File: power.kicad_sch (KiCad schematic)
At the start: 13 parts, among them P1 USB_C_Plug_USB2.0, Q1 FS8205A, U2 TP4056-42-ESOP8, U3 DW01A

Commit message: update
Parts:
- C1, C2: footprint (none) -> Capacitor_SMD:C_0805_2012Metric_Pad1.18x1.45mm_HandSolder
- D85, D86: footprint (none) -> LED_SMD:LED_0805_2012Metric_Pad1.15x1.40mm_HandSolder
- P1: footprint (none) -> Connector_USB:USB_C_Receptacle_GCT_USB4105-xx-A_16P_TopMnt_Horizontal
- R1, R2, R3, R4, R5: footprint (none) -> Resistor_SMD:R_0805_2012Metric_Pad1.20x1.40mm_HandSolder

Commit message: almost done
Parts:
- added D87: LED, LED_SMD:LED_0805_2012Metric_Pad1.15x1.40mm_HandSolder, symbol Device:LED
- added J3: Conn_01x02_Pin, Connector_JST:JST_PH_B2B-PH-K_1x02_P2.00mm_Vertical, symbol Connector:Conn_01x02_Pin
- added R7: 1k, Resistor_SMD:R_0805_2012Metric_Pad1.20x1.40mm_HandSolder, symbol Device:R
- added SW88: SW_SPDT, Button_Switch_THT:SW_Slide_SPDT_Angled_CK_OS102011MA1Q, symbol Switch:SW_SPDT
- added U4: MCP1700x-330xxTT, Package_TO_SOT_SMD:SOT-23W_Handsoldering, symbol Regulator_Linear:MCP1700x-330xxTT
- C2: value C -> 0.1u
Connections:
- net B- is gone; now on net -BATT: C1.2, Q1.2, Q1.3, U3.6 (GND)
- net VCC is gone; now on net +BATT: R1.1
- net +BATT: now also U2.5 (BAT), J3.1 (Pin_1), SW88.2 (B)
- net -BATT: now also J3.2 (Pin_2)
- net GND: now also R7.2, U4.1 (GND)
- net USB_D+: now reaches P1.A6 (D+)
- net USB_D-: now reaches P1.A7 (D-)
- new net: SW88.1 (A), U4.3 (VI)
- new net: D87.1 (K), R7.1
- new net +3.3V: D87.2 (A), U4.2 (VO)

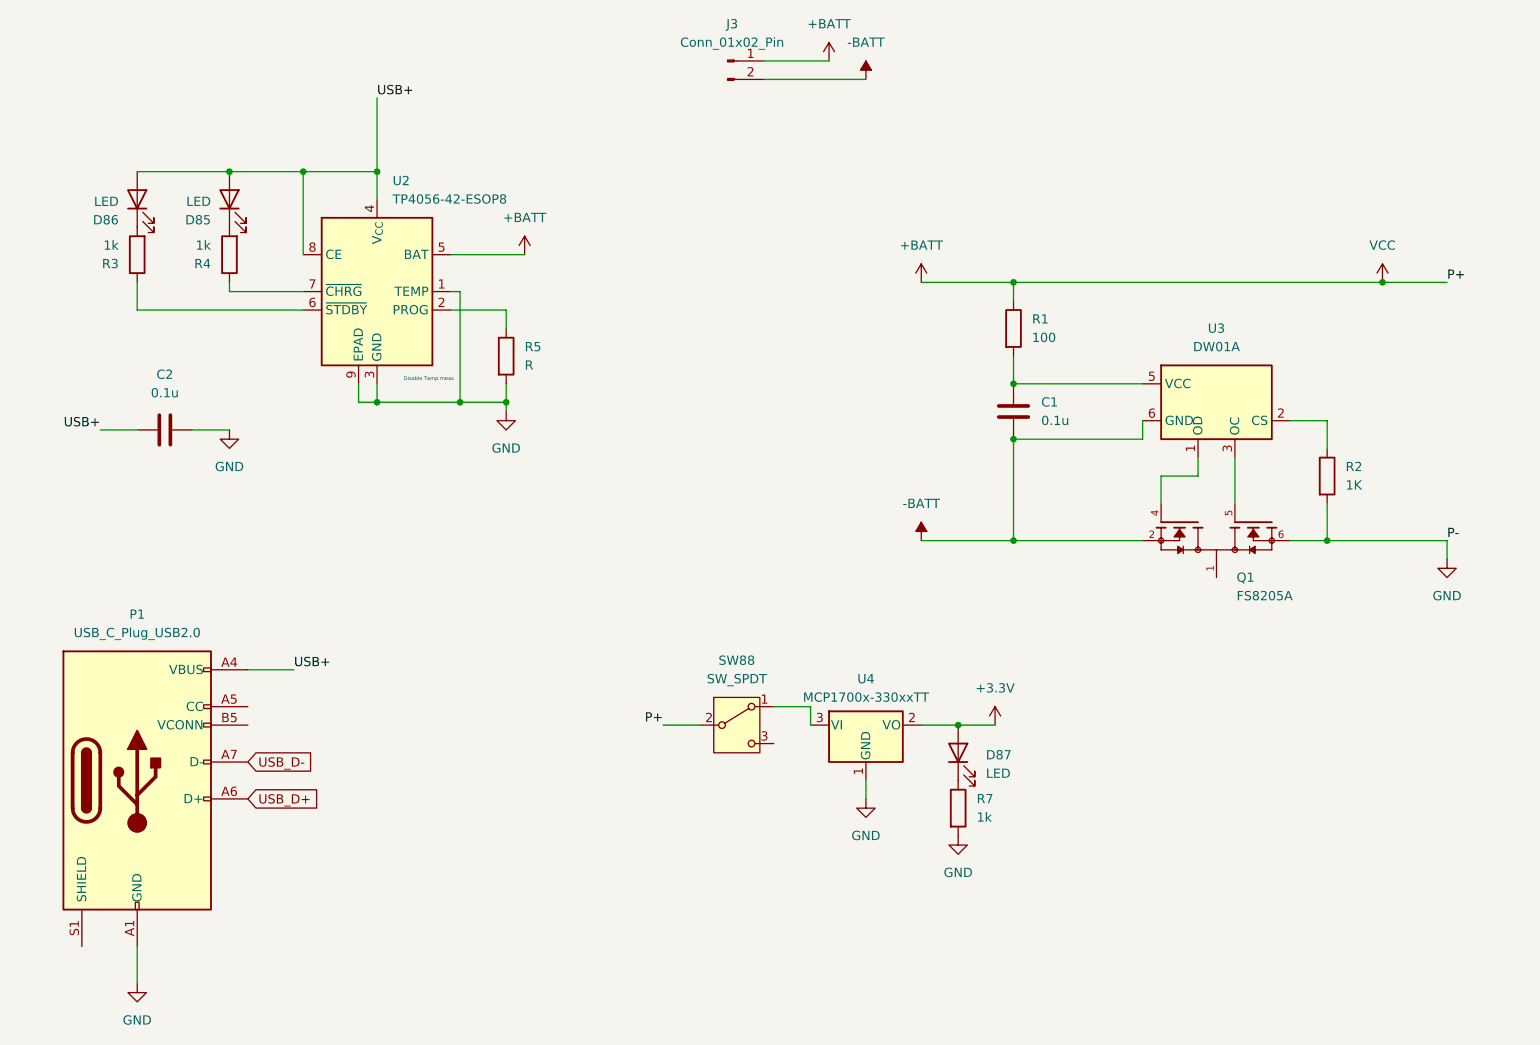
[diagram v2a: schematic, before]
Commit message: added more leds pins, fixed rule errors.
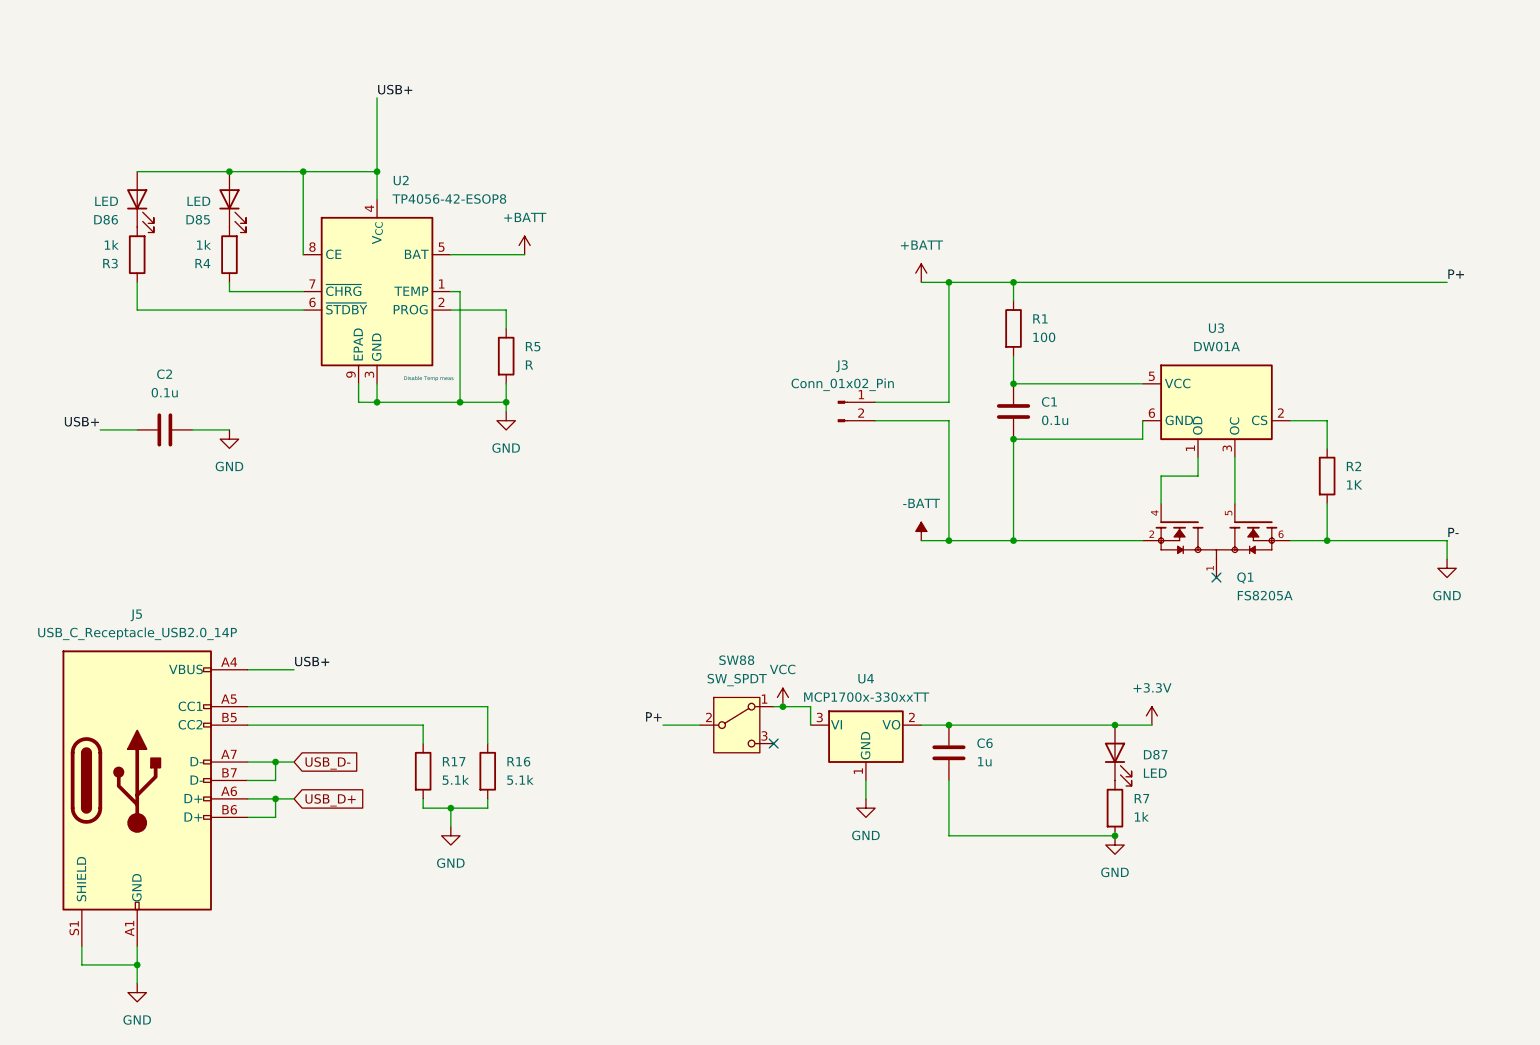
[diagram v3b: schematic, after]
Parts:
- removed P1: USB_C_Plug_USB2.0, Connector_USB:USB_C_Receptacle_GCT_USB4105-xx-A_16P_TopMnt_Horizontal, symbol Connector:USB_C_Plug_USB2.0
- added C6: 1u, Capacitor_SMD:C_0805_2012Metric_Pad1.18x1.45mm_HandSolder, symbol Device:C
- added J5: USB_C_Receptacle_USB2.0_14P, symbol Connector:USB_C_Receptacle_USB2.0_14P
- added R16, R17: 5.1k, Resistor_SMD:R_0805_2012Metric_Pad1.20x1.40mm_HandSolder, symbol Device:R
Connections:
- net +3.3V: now also C6.1
- net GND: now also C6.2, J5.A1 (GND), J5.A12 (GND), J5.B1 (GND), J5.B12 (GND), J5.S1 (SHIELD), R16.2, R17.2
- net USB+: now also J5.A4 (VBUS), J5.A9 (VBUS), J5.B4 (VBUS), J5.B9 (VBUS)
- net USB_D+: now also J5.A6 (D+), J5.B6 (D+)
- net USB_D-: now also J5.A7 (D-), J5.B7 (D-)
- net VCC: now reaches SW88.1 (A), U4.3 (VI)
- new net: J5.A5 (CC1), R16.1
- new net: J5.B5 (CC2), R17.1
- no-connect marks 0 -> 2
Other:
- moved on the sheet: D87, J3, R7

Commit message: udate
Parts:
- J5: footprint (none) -> Connector_USB:USB_C_Receptacle_GCT_USB4105-xx-A_16P_TopMnt_Horizontal
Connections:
- net VCC: no longer names the net of SW88.1 (A), U4.3 (VI)
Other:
- moved on the sheet: C2

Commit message: sent to fab
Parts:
- removed U4: MCP1700x-330xxTT, Package_TO_SOT_SMD:SOT-23W_Handsoldering, symbol Regulator_Linear:MCP1700x-330xxTT
- added C7: 22uf, Capacitor_SMD:C_0603_1608Metric_Pad1.08x0.95mm_HandSolder, symbol Device:C
- added C8: 10uf, Capacitor_SMD:C_0603_1608Metric_Pad1.08x0.95mm_HandSolder, symbol Device:C
- added U4: AP2112K-3.3, Package_TO_SOT_SMD:SOT-23-5, symbol Regulator_Linear:AP2112K-3.3
- C6: value 1u -> 0.1uf; footprint Capacitor_SMD:C_0805_2012Metric_Pad1.18x1.45mm_HandSolder -> Capacitor_SMD:C_0603_1608Metric_Pad1.08x0.95mm_HandSolder
- Q1: footprint FS8205A:SOP65P640X120-8N -> Package_TO_SOT_SMD:SOT-23-6
- R16, R17: footprint Resistor_SMD:R_0805_2012Metric_Pad1.20x1.40mm_HandSolder -> Resistor_SMD:R_0603_1608Metric_Pad0.98x0.95mm_HandSolder
- R2: value 1K -> 1k
- R5: value R -> 1.2k
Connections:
- net +3.3V: now also C7.1, U4.5 (VOUT)
- net GND: now also C7.2, C8.2, U4.2 (GND)
- net at SW88.1 (A): now also C8.1, U4.1 (VIN), U4.3 (EN)
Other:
- note added: "Charging Circuit"
- note added: "Voltage Protection"
- moved on the sheet: C6, D87, R7, SW88
